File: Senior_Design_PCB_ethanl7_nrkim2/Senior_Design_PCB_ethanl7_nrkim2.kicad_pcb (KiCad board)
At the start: 2 copper layers, 83 parts, among them J1 Piezo, J10 M6, J2 9V supply battery or bench, J3 Conn_02x03_Odd_Even, J4 Conn_ARM_JTAG_SWD_10, J5 M1, J6 M2, J7 M3, J8 M4, J9 M5, SW1 SW_Push, U1 uA7805, U2 LM386, U3 L298N, U4 L298N, U5 L298N, U6 STM32H7B0RBTx, U7 LM2937xT

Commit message: finished v1 pcb design
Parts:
- added C19: 100 nF, Capacitor_SMD:C_0805_2012Metric_Pad1.18x1.45mm_HandSolder, F.Cu at (165.4, 125.2)
- added R11: 10 kOhm, Resistor_SMD:R_0805_2012Metric_Pad1.20x1.40mm_HandSolder, F.Cu at (177.8, 139.2)
- added R12: 20 kOhm, Resistor_SMD:R_0805_2012Metric_Pad1.20x1.40mm_HandSolder, F.Cu at (181.3, 139.2)
- D1, D2: footprint LED_SMD:LED_0805_2012Metric_Pad1.15x1.40mm_HandSolder -> Connector_Molex:Molex_KK-254_AE-6410-02A_1x02_P2.54mm_Vertical
- moved J2 122.3 mm to (197.3, 39.5), turned to 0 degrees
- moved C2 104.1 mm to (193.3, 52.8), turned to 0 degrees
- moved TP4 102.0 mm to (190.6, 46.6), turned to 90 degrees
- moved C1 100.2 mm to (198.8, 58.3), turned to 180 degrees
- moved C3 91.2 mm to (183.6, 67.6), turned to 0 degrees
- moved U1 88.2 mm to (187.9, 57.9), turned to 90 degrees
- moved C4 86.7 mm to (188.7, 72.1), turned to 0 degrees
- moved U7 84.3 mm to (194.3, 67.0), turned to -90 degrees
- moved TP5 74.1 mm to (191.0, 77.1), turned to -90 degrees
- moved H1 67.4 mm to (84.8, 30.2)
- moved C12 55.8 mm to (177.5, 87.4), turned to 0 degrees
- moved D11 54.0 mm to (174.5, 36.8), turned to -90 degrees
- moved R5 51.1 mm to (177.5, 89.9), turned to 180 degrees
- moved SW1 50.6 mm to (183.0, 81.6)
- moved D27 44.3 mm to (128.4, 37.1), turned to -90 degrees
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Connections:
- TP2 pad 1: /Amp_Sig -> Net-(R11-Pad1)
- U2 pad 5: /Amp_Sig -> Net-(R11-Pad1)
- U2 pad 6: +5V -> Net-(U2-V+)
- U6 pad 27: /M1P -> /M5P
- U6 pad 28: /M1N -> /M5N
- U6 pad 29: /M2P -> /M6P
- U6 pad 33: /M2N -> /M6N
- U6 pad 35: /M3P -> /M1P
- U6 pad 36: /M3N -> /M1N
- U6 pad 37: /M4P -> /M2P
- U6 pad 38: /M4N -> /M2N
- U6 pad 41: /M5P -> /M3P
- U6 pad 42: /M5N -> /M3N
- U6 pad 51: /M6P -> /M4P
- U6 pad 52: /M6N -> /M4N
- U6 pad 57: Net-(D1-A) -> Net-(D2-A)
- U6 pad 58: Net-(D2-A) -> Net-(D1-A)
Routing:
- net +5V: track 0.00 -> 436.3 mm
- net GND: track 0.00 -> 339.5 mm, vias 0 -> 12
- net +3.3V: track 0.00 -> 204.3 mm
- net +9V: track 0.00 -> 193.7 mm, vias 0 -> 6
- net /M6N: track 0.00 -> 85.6 mm, vias 0 -> 1
- net /Amp_Sig: track 0.00 -> 80.0 mm
- net Net-(D17-A): track 0.00 -> 53.8 mm
- net /M6P: track 0.00 -> 53.7 mm, vias 0 -> 2
- net Net-(D13-A): track 0.00 -> 53.0 mm
- net Net-(D19-A): track 0.00 -> 53.0 mm
- net /M5N: track 0.00 -> 52.9 mm, vias 0 -> 1
- net /M5P: track 0.00 -> 52.6 mm, vias 0 -> 1
- net /M5En: track 0.00 -> 50.8 mm, vias 0 -> 1
- net Net-(D21-A): track 0.00 -> 50.5 mm
- net Net-(D23-A): track 0.00 -> 49.5 mm
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- added copper zone on B.Cu, net GND
- added copper zone on F.Cu, net GND
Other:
- board outline added: 127 x 127 mm
- board text added: "Automatic Guitar Tuner V1 03/31/25 Team 65"

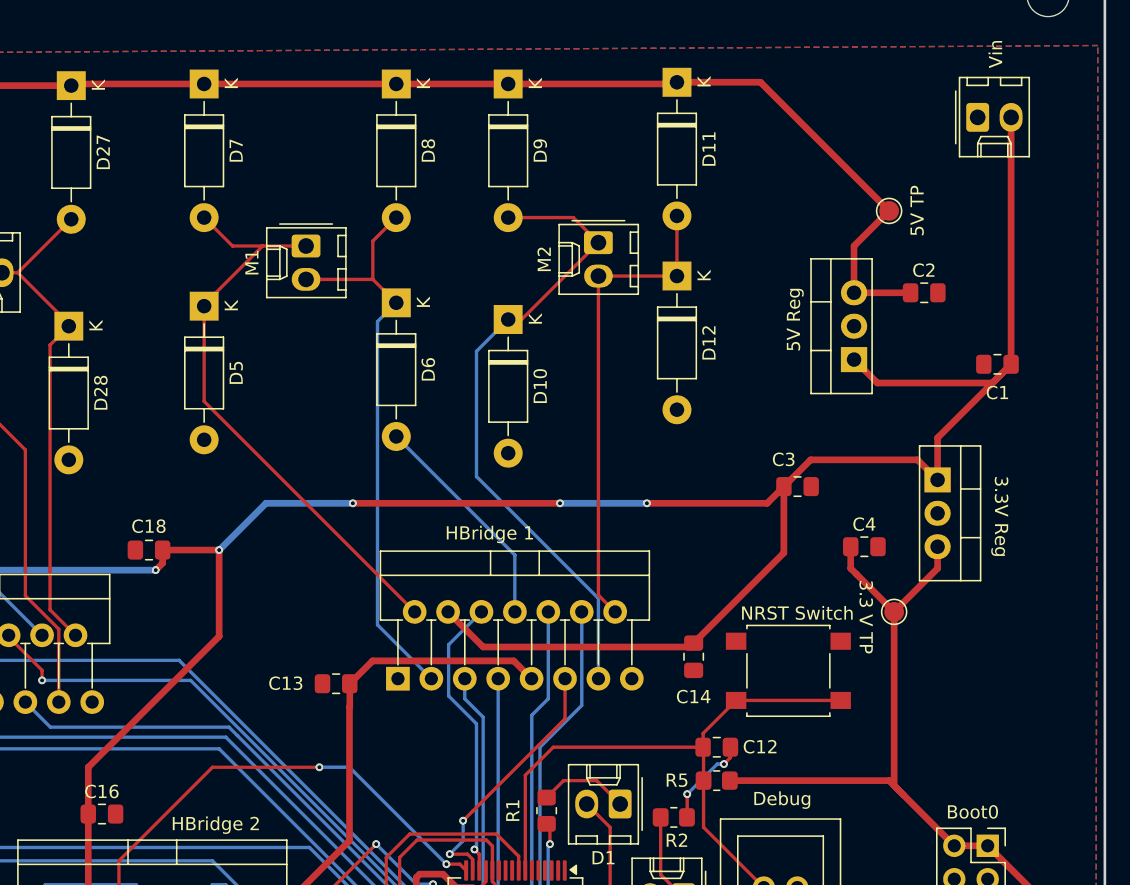
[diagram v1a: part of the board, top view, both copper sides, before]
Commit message: tweaked PCB layout
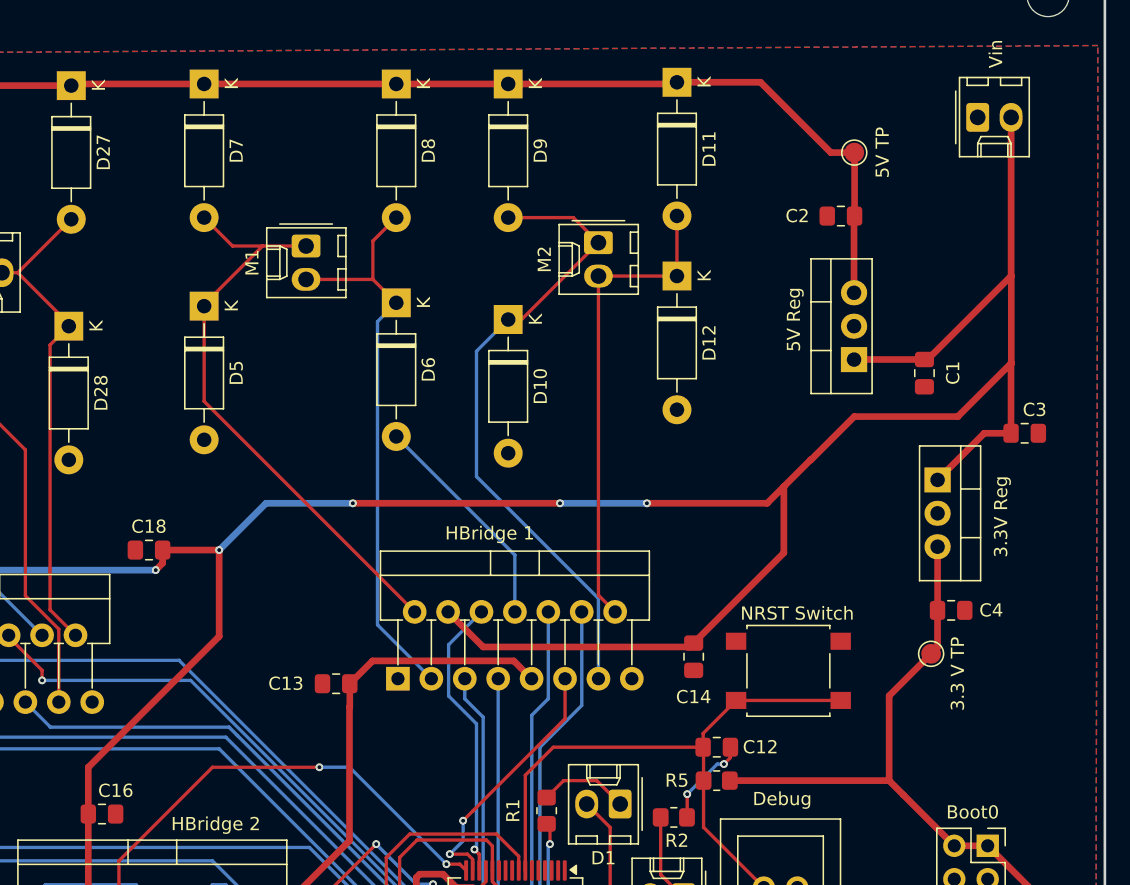
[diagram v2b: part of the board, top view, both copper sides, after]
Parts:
- moved C3 17.7 mm to (200.9, 63.5)
- moved C2 8.61 mm to (186.9, 47.0), turned to 180 degrees
- moved C4 8.18 mm to (195.3, 77.0)
- moved C1 5.59 mm to (193.3, 58.9), turned to -90 degrees
- moved TP4 5.17 mm to (188.0, 42.2)
- moved TP5 4.25 mm to (193.8, 80.3)
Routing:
- net +9V: track 193.7 -> 204.3 mm
- net +3.3V: track 204.3 -> 196.8 mm
- net +5V: track 436.3 -> 430.9 mm

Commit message: V1.1 pcb
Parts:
- moved D17 25.3 mm to (109.0, 100.1), turned to -90 degrees
- moved D15 20.6 mm to (105.7, 115.3)
- moved D13 20.6 mm to (105.7, 127.5)
- moved D19 19.2 mm to (103.6, 90.7), turned to -90 degrees
- moved D22 19.0 mm to (106.4, 58.2)
- moved D21 19.0 mm to (106.6, 40.4)
- moved D23 19.0 mm to (119.7, 40.4)
- moved D24 19.0 mm to (119.6, 58.4)
- moved J9 19.0 mm to (112.4, 54.6)
- moved H1 16.9 mm to (100.8, 35.6), turned to 180 degrees
- moved J8 16.8 mm to (116.6, 101.3)
- moved J7 16.8 mm to (116.3, 122.2)
- moved D16 16.3 mm to (122.2, 115.1)
- moved D14 16.3 mm to (122.4, 127.3)
- moved H3 16.2 mm to (100.8, 142.2)
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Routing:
- net +5V: track 430.9 -> 339.1 mm, vias 0 -> 2
- net /M6N: track 85.6 -> 50.6 mm, vias 1 -> 3
- net GND: track 339.5 -> 317.1 mm, vias 12 -> 14
- net Net-(D15-A): track 41.4 -> 26.5 mm
- net Net-(D21-A): track 50.5 -> 37.5 mm
- net Net-(D17-A): track 53.8 -> 41.0 mm
- net Net-(D13-A): track 53.0 -> 41.3 mm
- net Net-(D23-A): track 49.5 -> 40.3 mm
- net Net-(D5-K): track 44.9 -> 36.3 mm
- net Net-(D10-K): track 49.1 -> 42.8 mm
- net Net-(D25-A): track 47.0 -> 40.9 mm
- net +9V: track 204.3 -> 199.0 mm
- net Net-(D6-K): track 43.9 -> 40.3 mm
- net Net-(D19-A): track 53.0 -> 49.6 mm
- net Net-(U2-V+): track 13.9 -> 16.9 mm, vias 0 -> 1
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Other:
- board size 127 x 127 mm -> 111.5 x 116.1 mm
- board text added: "Automatic Guitar Tuner V1.1 04/07/25 Team 65"
- board text removed: "Automatic Guitar Tuner V1 03/31/25 Team 65"
